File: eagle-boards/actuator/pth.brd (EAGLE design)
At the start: 59.4 x 53.3 mm, 12 parts, among them IC1 ULN2003AN, IC2 ULN2003AN

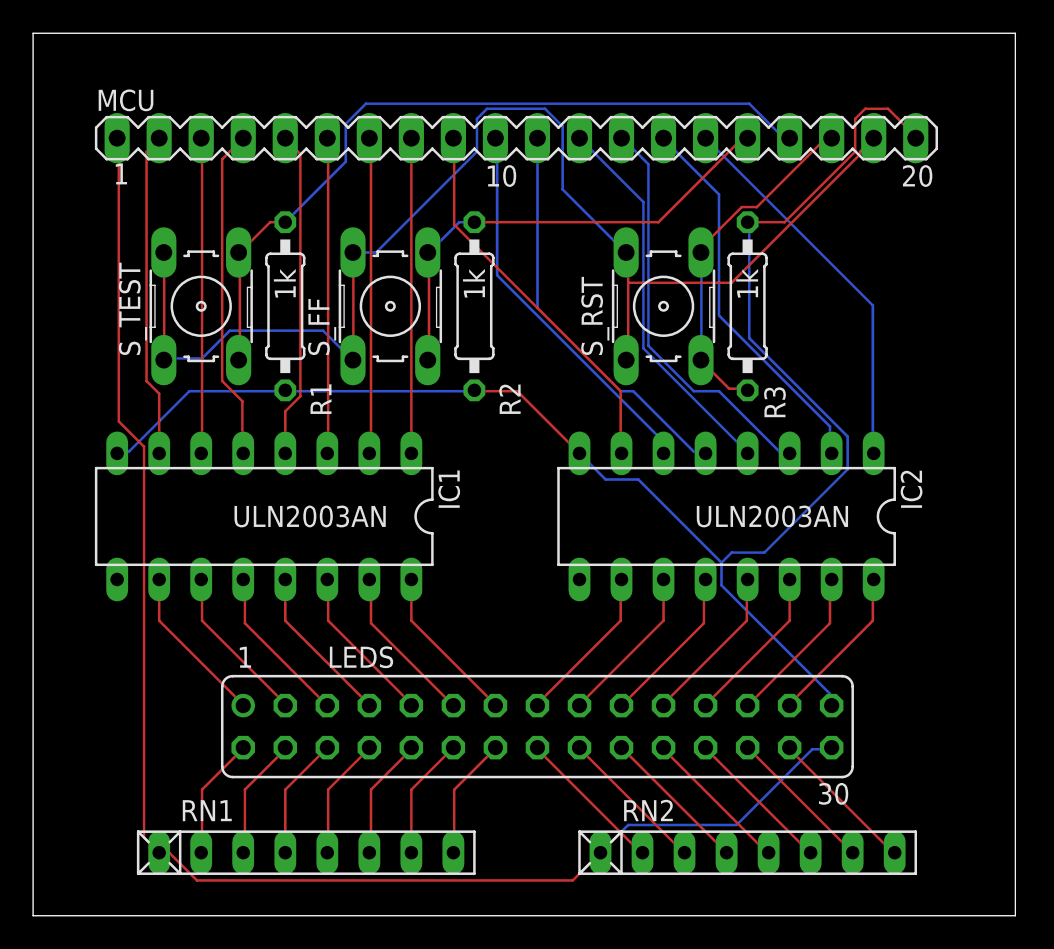
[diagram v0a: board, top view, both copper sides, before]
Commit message: Add a new revision for the actuator board.
Rotate the board so that the writing is in the same orientation as the controller board once mounted.

Include +5/GND markings on both connectors.

Put the MCU connector on the _bottom_ layer, rather than the top.
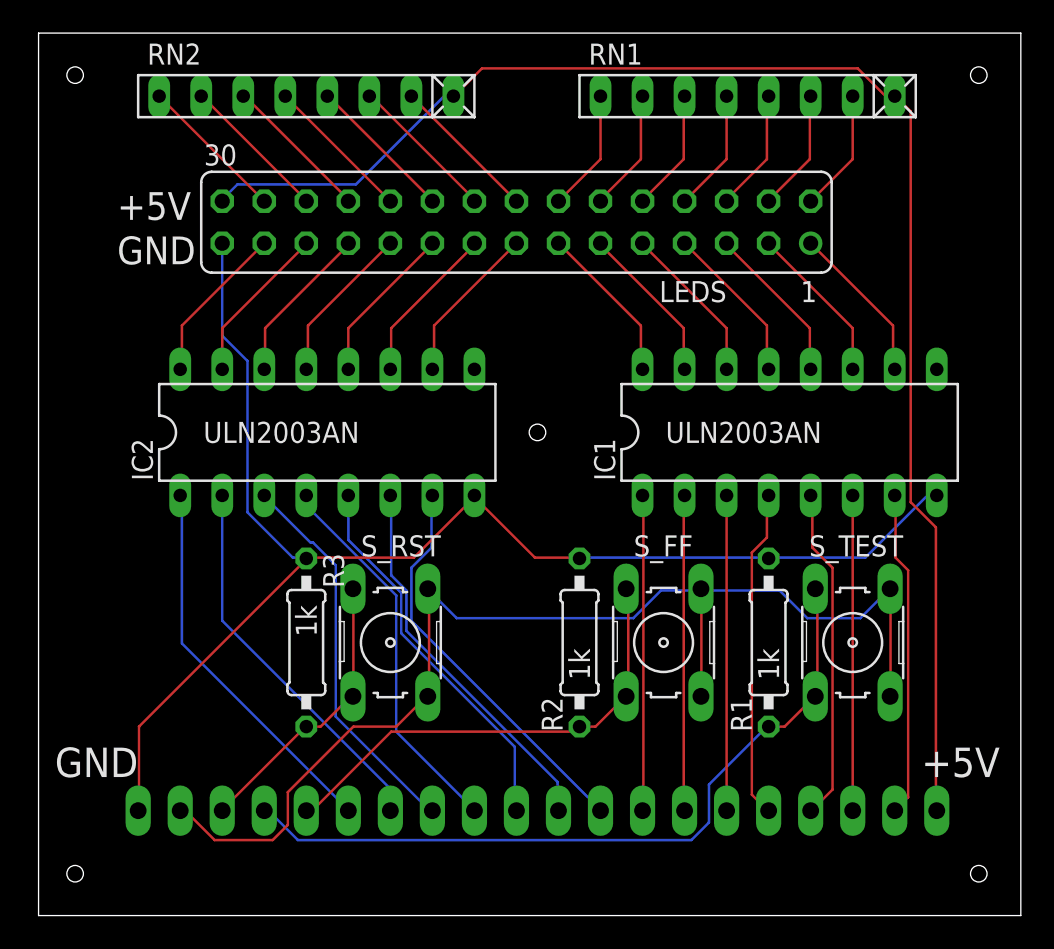
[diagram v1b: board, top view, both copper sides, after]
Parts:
- removed MCU: (no value), con-lstb:MA20-1
- added MCU1: (no value), con-lstb:MA20-1
- moved RN1 52.9 mm to (43.2, 49.5), turned to 180 degrees
- moved RN2 52.9 mm to (16.5, 49.5), turned to 180 degrees
- moved S_TEST 44.3 mm to (49.5, 16.5), turned to 270 degrees
- moved R1 35.6 mm to (44.5, 16.5), turned to 90 degrees
- moved R3 33.5 mm to (16.5, 16.5)
- moved IC1 32.2 mm to (45.7, 29.2), turned to 0 degrees
- moved LEDS 30.5 mm to (29.2, 41.9), turned to 180 degrees
- moved S_FF 26.2 mm to (38.1, 16.5), turned to 270 degrees
- moved S_RST 26.2 mm to (21.6, 16.5), turned to 270 degrees
- moved IC2 24.7 mm to (17.8, 29.2), turned to 0 degrees
- moved R2 21.3 mm to (33.0, 16.5), turned to 90 degrees
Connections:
- net GND: now also MCU1.20; no longer MCU.20
- net N$1: now also MCU1.8; no longer MCU.8
- net N$10: now also MCU1.10; no longer MCU.10
- net N$11: now also MCU1.11; no longer MCU.11
- net N$12: now also MCU1.12; no longer MCU.12
- net N$13: now also MCU1.13; no longer MCU.13
- net N$14: now also MCU1.14; no longer MCU.14
- net N$15: now also MCU1.15; no longer MCU.15
- net N$17: now also MCU1.18; no longer MCU.18
- net N$18: now also MCU1.17; no longer MCU.17
- net N$19: now also MCU1.16; no longer MCU.16
- net N$2: now also MCU1.19; no longer MCU.19
- net N$3: now also MCU1.2; no longer MCU.2
- net N$4: now also MCU1.3; no longer MCU.3
- net N$5: now also MCU1.4; no longer MCU.4
- net N$6: now also MCU1.5; no longer MCU.5
- net N$7: now also MCU1.6; no longer MCU.6
- net N$8: now also MCU1.7; no longer MCU.7
- net N$9: now also MCU1.9; no longer MCU.9
- net VCC: now also MCU1.1; no longer MCU.1
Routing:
- net GND: track 96.3 -> 83.9 mm
- net N$2: track 78.3 -> 71.0 mm
- net N$17: track 21.1 -> 17.3 mm
- net N$9: track 23.2 -> 24.3 mm
- net N$13: track 24.5 -> 23.5 mm
- net N$11: track 24.1 -> 23.3 mm
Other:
- board text added: "+5V"
- board text added: "+5V GND"
- board text added: "Birch Books Smart Home - Actuator Board (PTH) rev.3"
- board text added: "Copyright © 2020 D. E. Pettenò flameeyes.com/p/birch-books Licensed under MIT License"
- board text added: "GND"
- board text removed: "Birch Books Smart Home - Actuator Board (PTH) rev.2"
- board text removed: "Copyright © 2020 D. E. Pettenò - flameeyes.com/p/birch-books Licensed under MIT License"
